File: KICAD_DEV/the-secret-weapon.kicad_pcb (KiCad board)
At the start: 6 copper layers, 100 x 100 mm, 45 parts, among them J1 USB_C_Receptacle_USB2.0_14P, J2 Screw_Terminal_01x02, SW1 SW_Push, SW2 SW_Push, U1 STM32H743VITx, U2 USBLC6-2SC6, U3 LMR33640ADDA, U4 LM1086S-3.3/TR, Y1 8 MHz, Y2 32.768 KHz

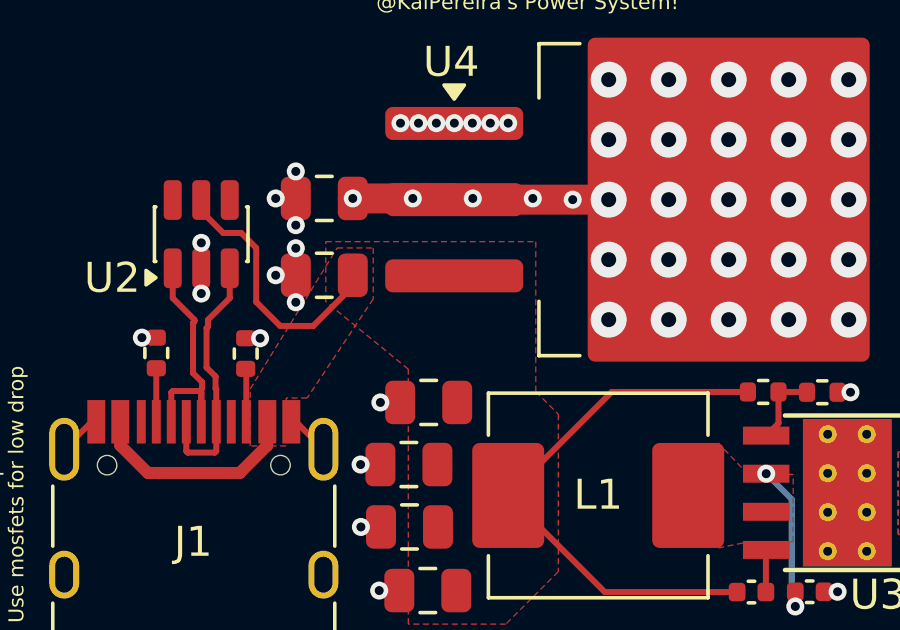
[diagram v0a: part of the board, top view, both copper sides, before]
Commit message: adjusting the power fills and adding the power rails!
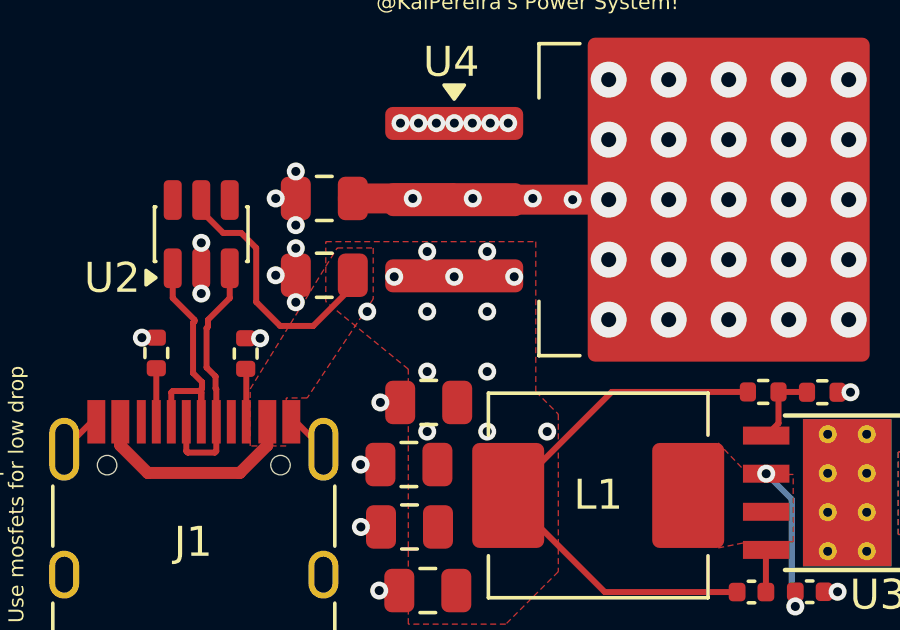
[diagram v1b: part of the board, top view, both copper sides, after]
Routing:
- net +12V: track 1.12 -> 119.7 mm
- net +5V: track 34.6 -> 100.9 mm, vias 0 -> 13
- net +3V3: vias 40 -> 39
- added copper zone on In2.Cu, net +5V
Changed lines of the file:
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@@
-	)
-	(via
-		(at 129.32 164.05)
-		(size 0.6)
-		(drill 0.3)
-		(layers "F.Cu" "B.Cu")
-		(net 9)
 	)
 	(via
@@
 		(net 90)
 	)
+	(via
+		(at 131.8 171.82)
+		(size 0.6)
+		(drill 0.3)
+		(layers "F.Cu" "B.Cu")
+		(net 90)
+	)
+	(via
+		(at 131.8 167.82)
+		(size 0.6)
+		(drill 0.3)
+		(layers "F.Cu" "B.Cu")
+		(net 90)
+	)
+	(via
+		(at 133.8 171.82)
+		(size 0.6)
+		(drill 0.3)
+		(layers "F.Cu" "B.Cu")
+		(net 90)
+	)
+	(via
+		(at 129.8 167.82)
+		(size 0.6)
+		(drill 0.3)
+		(layers "F.Cu" "B.Cu")
+		(net 90)
+	)
+	(via
+		(at 133.8 169.82)
+		(size 0.6)
+		(drill 0.3)
+		(layers "F.Cu" "B.Cu")
+		(net 90)
+	)
+	(via
+		(at 133.8 167.82)
+		(size 0.6)
+		(drill 0.3)
+		(layers "F.Cu" "B.Cu")
+		(net 90)
+	)
+	(via
+		(at 131.8 165.82)
+		(size 0.6)
+		(drill 0.3)
+		(layers "F.Cu" "B.Cu")
+		(net 90)
+	)
+	(via
+		(at 131.8 169.82)
+		(size 0.6)
+		(drill 0.3)
+		(layers "F.Cu" "B.Cu")
+		(net 90)
+	)
+	(via
+		(at 130.7 166.66)
+		(size 0.6)
+		(drill 0.3)
+		(layers "F.Cu" "B.Cu")
+		(net 90)
+	)
+	(via
+		(at 134.7 166.66)
+		(size 0.6)
+		(drill 0.3)
+		(layers "F.Cu" "B.Cu")
+		(net 90)
+	)
+	(via
+		(at 135.8 171.82)
+		(size 0.6)
+		(drill 0.3)
+		(layers "F.Cu" "B.Cu")
+		(net 90)
+	)
+	(via
+		(at 132.7 166.66)
+		(size 0.6)
+		(drill 0.3)
+		(layers "F.Cu" "B.Cu")
+		(net 90)
+	)
+	(via
+		(at 133.8 165.82)
+		(size 0.6)
+		(drill 0.3)
+		(layers "F.Cu" "B.Cu")
+		(net 90)
+	)
+	(segment
+		(start 131.807265 166.66)
+		(end 128.92 163.772735)
+		(width 2)
+		(layer "In2.Cu")
+		(net 90)
+	)
+	(segment
+		(start 124.69 155.52)
+		(end 118.78 155.52)
+		(width 2)
+		(layer "In2.Cu")
+		(net 90)
+	)
+	(segment
+		(start 109.91 146.65)
+		(end 109.91 115.82)
+		(width 2)
+		(layer "In2.Cu")
+		(net 90)
+	)
+	(segment
+		(start 128.92 159.75)
+		(end 128.7 159.53)
+		(width 2)
+		(layer "In2.Cu")
+		(net 90)
+	)
+	(segment
+		(start 134.7 166.66)
+		(end 131.807265 166.66)
+		(width 2)
+		(layer "In2.Cu")
+		(net 90)
+	)
+	(segment
+		(start 118.78 155.52)
+		(end 109.91 146.65)
+		(width 2)
+		(layer "In2.Cu")
+		(net 90)
+	)
+	(segment
+		(start 128.92 163.772735)
+		(end 128.92 159.75)
+		(width 2)
+		(layer "In2.Cu")
+		(net 90)
+	)
+	(segment
+		(start 128.7 159.53)
+		(end 124.69 155.52)
+		(width 2)
+		(layer "In2.Cu")
+		(net 90)
+	)
 	(segment
 		(start 124.221 170.469)
@@
 		(layers "F.Cu" "B.Cu")
 		(free yes)
+		(net 94)
+	)
+	(segment
+		(start 150.9 96.09)
+		(end 115.68 96.09)
+		(width 3)
+		(layer "In2.Cu")
+		(net 94)
+	)
+	(segment
+		(start 156.04 162.75)
+		(end 162.1 156.69)
+		(width 3)
+		(layer "In2.Cu")
+		(net 94)
+	)
+	(segment
+		(start 156.04 165.25)
+		(end 156.04 162.75)
+		(width 3)
+		(layer "In2.Cu")
+		(net 94)
+	)
+	(segment
+		(start 162.1 156.69)
+		(end 162.1 107.29)
+		(width 3)
+		(layer "In2.Cu")
+		(net 94)
+	)
+	(segment
+		(start 162.1 107.29)
+		(end 150.9 96.09)
+		(width 3)
+		(layer "In2.Cu")
+		(net 94)
+	)
+	(segment
+		(start 156.04 162.75)
+		(end 159.54 162.75)
+		(width 3)
+		(layer "In2.Cu")
+		(net 94)
+	)
+	(segment
+		(start 159.54 165.25)
+		(end 156.04 165.25)
+		(width 3)
+		(layer "In2.Cu")
 		(net 94)
 	)
@@
 			(pts
 				(xy 141.5 172.2) (xy 141.5 175.7) (xy 142.5 175.5) (xy 144 175.5) (xy 144 173.25) (xy 142.5 173.25)
-			)
-		)
-	)
-	(zone
-		(net 90)
-		(net_name "+5V")
-		(layer "F.Cu")
-		(hatch edge 0.5)
-		(priority 5)
-		(connect_pads
-			(clearance 0.1)
-		)
-		(min_thickness 0.25)
-		(filled_areas_thickness no)
-		(fill yes
-			(thermal_gap 0.3)
-			(thermal_bridge_width 0.5)
-		)
-		(polygon
-			(pts
-				(xy 125.9 172.3) (xy 125.9 170.4) (xy 128.8 165.7) (xy 130 165.7) (xy 130 167.4) (xy 127.8 170.7)
-				(xy 127.1 170.7) (xy 127.1 172.3)
-			)
-		)
-	)
-	(zone
-		(net 90)
-		(net_name "+5V")
-		(layer "F.Cu")
-		(hatch edge 0.5)
-		(priority 3)
-		(connect_pads
-			(clearance 0.2)
-		)
-		(min_thickness 0.25)
-		(filled_areas_thickness no)
-		(fill yes
-			(thermal_gap 0.15)
-			(thermal_bridge_width 1)
-		)
-		(polygon
-			(pts
-				(xy 135.42 165.49) (xy 135.42 170.49) (xy 136.17 171.24) (xy 136.17 176.49) (xy 134.42 178.24) (xy 131.17 178.24)
-				(xy 131.17 169.74) (xy 128.42 167.49) (xy 128.42 165.49)
 			)
 		)
@@
 	)
 	(zone
+		(net 90)
+		(net_name "+5V")
+		(layers "F.Cu" "In2.Cu")
+		(hatch edge 0.5)
+		(priority 5)
+		(connect_pads
+			(clearance 0.1)
+		)
+		(min_thickness 0.25)
+		(filled_areas_thickness no)
+		(fill yes
+			(thermal_gap 0.3)
+			(thermal_bridge_width 0.5)
+		)
+		(polygon
+			(pts
+				(xy 125.9 172.3) (xy 125.9 170.4) (xy 128.8 165.7) (xy 130 165.7) (xy 130 167.4) (xy 127.8 170.7)
+				(xy 127.1 170.7) (xy 127.1 172.3)
+			)
+		)
+	)
+	(zone
+		(net 90)
+		(net_name "+5V")
+		(layers "F.Cu" "In2.Cu")
+		(hatch edge 0.5)
+		(priority 3)
+		(connect_pads
+			(clearance 0.2)
+		)
+		(min_thickness 0.25)
+		(filled_areas_thickness no)
+		(fill yes
+			(thermal_gap 0.15)
+			(thermal_bridge_width 1)
+		)
+		(polygon
+			(pts
+				(xy 135.42 165.49) (xy 135.42 170.49) (xy 136.17 171.24) (xy 136.17 176.49) (xy 134.42 178.24) (xy 131.17 178.24)
+				(xy 131.17 169.74) (xy 128.42 167.49) (xy 128.42 165.49)
+			)
+		)
+	)
+	(zone
 		(net 1)
 		(net_name "GND")
@@
 		(hatch edge 0.5)
 		(connect_pads
-			(clearance 0.5)
+			(clearance 0.2)
 		)
 		(min_thickness 0.25)
@@
 		(fill yes
 			(thermal_gap 0.5)
-			(thermal_bridge_width 0.5)
+			(thermal_bridge_width 1)
 		)
 		(polygon
@@
 		(hatch edge 0.5)
 		(connect_pads
-			(clearance 0.5)
+			(clearance 0.3)
 		)
 		(min_thickness 0.25)

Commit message: forgot to wire USB data pairs, doing that now!
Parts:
- moved C24 27.7 mm to (125.3, 144.3), turned to 180 degrees
- moved C8 27.3 mm to (123.8, 142.3), turned to 180 degrees
- moved C29 26.9 mm to (126.8, 123.4), turned to -90 degrees
- moved R13 26.9 mm to (140.6, 122.1), turned to 0 degrees
- moved C7 26.8 mm to (138.5, 147.1), turned to -90 degrees
- moved R14 26.6 mm to (146.5, 127.9), turned to -90 degrees
- moved SW1 25.9 mm to (143.2, 124.3), turned to 180 degrees
- moved C21 25.5 mm to (140.5, 145.6), turned to -90 degrees
- moved Y1 23.3 mm to (130.3, 123.4), turned to 0 degrees
- moved C25 22.4 mm to (123.8, 131.8), turned to 180 degrees
- moved C27 22.4 mm to (139.9, 124.2), turned to 90 degrees
- moved C28 21.7 mm to (133.8, 123.4), turned to -90 degrees
- moved SW2 21.0 mm to (143.2, 128.0), turned to 0 degrees
- moved C30 19.5 mm to (138.9, 125.4), turned to -90 degrees
- moved C9 19.5 mm to (128.2, 127.0), turned to 90 degrees
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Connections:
- U1 pad 70: unconnected-(U1-PA11-Pad70) -> D-
- U1 pad 71: unconnected-(U1-PA12-Pad71) -> D+
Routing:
- net USB_D-: track 8.57 -> 2.99 mm
- net USB_D+: track 8.57 -> 2.99 mm
- net +5V: track 100.9 -> 100.0 mm

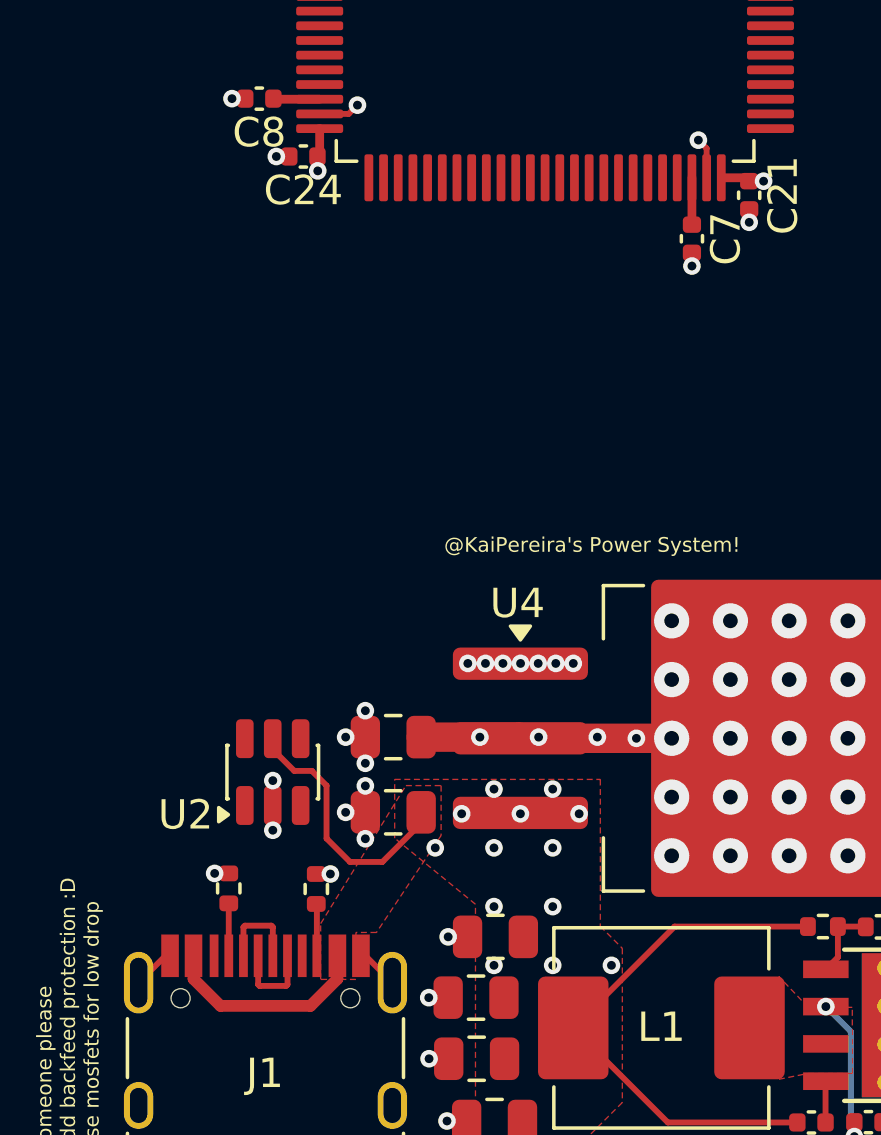
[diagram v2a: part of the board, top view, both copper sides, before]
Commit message: added some more warnings around the board and routed the USB data pairs!
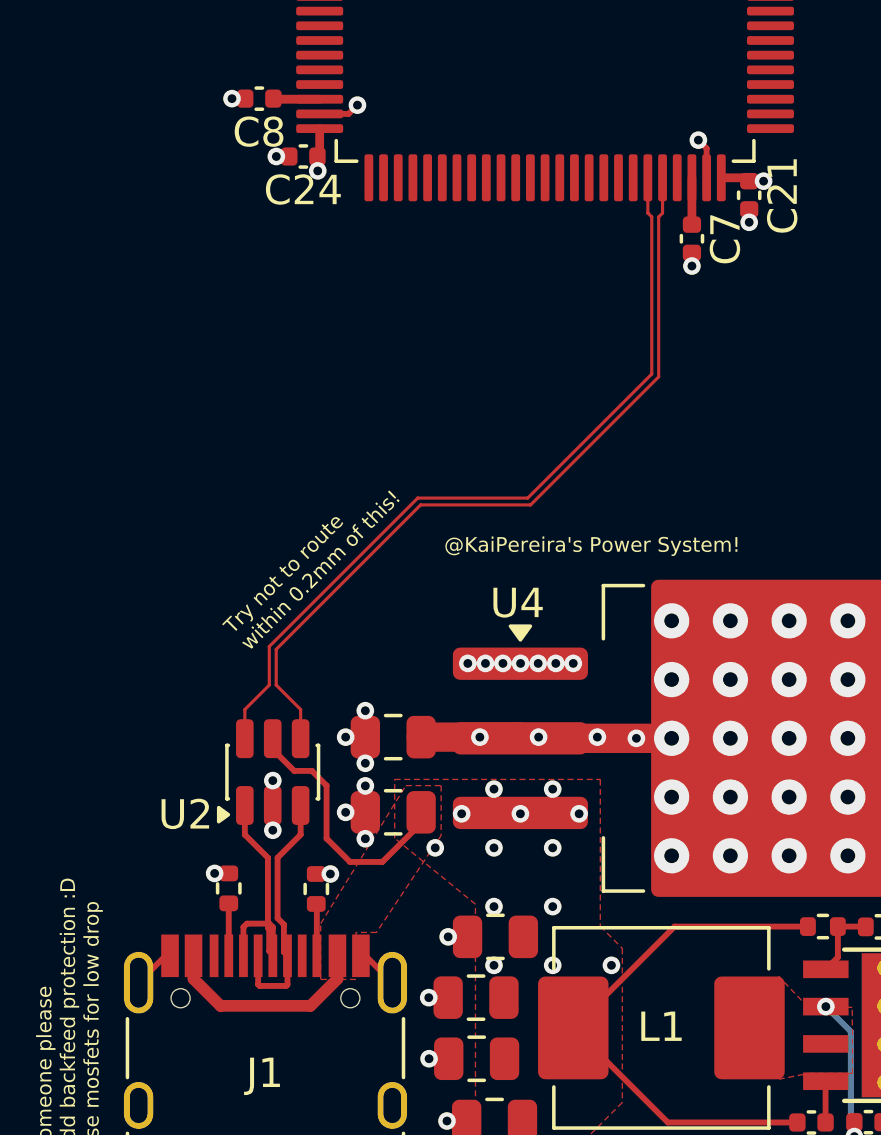
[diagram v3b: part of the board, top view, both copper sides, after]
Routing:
- net D-: track 0.00 -> 27.1 mm
- net D+: track 0.00 -> 27.1 mm
- net USB_D-: track 2.99 -> 8.59 mm
- net USB_D+: track 2.99 -> 8.58 mm
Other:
- board text added: "Try not to route within 0.2mm of this!"
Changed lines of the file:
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@@
 	)
 	(gr_text "Someone please \nadd backfeed protection :D\nUse mosfets for low drop"
-		(locked yes)
 		(at 118.4 178.2 90)
 		(layer "F.SilkS")
@@
 	)
 	(gr_text "Beginners can maybe \nadd some power LED's"
-		(locked yes)
 		(at 149.5 169.5 90)
 		(layer "F.SilkS")
@@
 	)
 	(gr_text "@KaiPereira's Power System!"
-		(locked yes)
 		(at 130.1 157.8 0)
 		(layer "F.SilkS")
@@
 		)
 	)
+	(gr_text "Try not to route \nwithin 0.2mm of this!"
+		(at 123.51 161.17 45)
+		(layer "F.SilkS")
+		(effects
+			(font
+				(size 0.5 0.5)
+				(thickness 0.1)
+			)
+			(justify left bottom)
+		)
+	)
 	(segment
 		(start 130.54 127.1)
@@
 	)
 	(segment
+		(start 124.648 171.373)
+		(end 124.648 170.432138)
+		(width 0.2)
+		(layer "F.Cu")
+		(net 87)
+	)
+	(segment
 		(start 123.77 172.472)
 		(end 123.77 171.495)
@@
 	)
 	(segment
+		(start 125.2175 167.371251)
+		(end 125.2175 166.3775)
+		(width 0.2)
+		(layer "F.Cu")
+		(net 87)
+	)
+	(segment
 		(start 124.77 171.495)
 		(end 124.77 172.472)
+		(width 0.2)
+		(layer "F.Cu")
+		(net 87)
+	)
+	(segment
+		(start 124.43198 170.216118)
+		(end 124.43198 168.156771)
+		(width 0.2)
+		(layer "F.Cu")
+		(net 87)
+	)
+	(segment
+		(start 124.77 171.495)
+		(end 124.648 171.373)
+		(width 0.2)
+		(layer "F.Cu")
+		(net 87)
+	)
+	(segment
+		(start 124.648 170.432138)
+		(end 124.43198 170.216118)
+		(width 0.2)
+		(layer "F.Cu")
+		(net 87)
+	)
+	(segment
+		(start 124.43198 168.156771)
+		(end 125.2175 167.371251)
 		(width 0.2)
 		(layer "F.Cu")
@@
 	)
 	(segment
-		(start 124.221 170.469)
-		(end 123.319 170.469)
+		(start 123.388 170.4)
+		(end 123.27 170.518)
 		(width 0.2)
 		(layer "F.Cu")
@@
 	)
 	(segment
-		(start 123.319 170.469)
-		(end 123.27 170.518)
+		(start 123.3175 167.371251)
+		(end 123.3175 166.3775)
+		(width 0.2)
+		(layer "F.Cu")
+		(net 89)
+	)
+	(segment
+		(start 124.27 171.495)
+		(end 124.27 171.457448)
 		(width 0.2)
 		(layer "F.Cu")
@@
 	)
 	(segment
+		(start 124.148 171.335448)
+		(end 124.148 170.542)
+		(width 0.2)
+		(layer "F.Cu")
+		(net 89)
+	)
+	(segment
+		(start 124.27 170.518)
+		(end 124.152 170.4)
+		(width 0.2)
+		(layer "F.Cu")
+		(net 89)
+	)
+	(segment
+		(start 124.104 170.542)
+		(end 124.104 168.157751)
+		(width 0.2)
+		(layer "F.Cu")
+		(net 89)
+	)
+	(segment
 		(start 123.27 170.518)
 		(end 123.27 171.495)
@@
 	)
 	(segment
-		(start 124.27 170.518)
-		(end 124.221 170.469)
+		(start 124.27 171.457448)
+		(end 124.148 171.335448)
 		(width 0.2)
 		(layer "F.Cu")
@@
 	)
 	(segment
+		(start 124.104 168.157751)
+		(end 123.3175 167.371251)
+		(width 0.2)
+		(layer "F.Cu")
+		(net 89)
+	)
+	(segment
+		(start 124.148 170.542)
+		(end 124.104 170.542)
+		(width 0.2)
+		(layer "F.Cu")
+		(net 89)
+	)
+	(segment
+		(start 124.152 170.4)
+		(end 123.388 170.4)
+		(width 0.2)
+		(layer "F.Cu")
+		(net 89)
+	)
+	(segment
+		(start 123.3175 163.108749)
+		(end 124.1504 162.275849)
+		(width 0.1072)
+		(layer "F.Cu")
+		(net 90)
+	)
+	(segment
+		(start 137.1729 146.337901)
+		(end 137.04 146.205001)
+		(width 0.1072)
+		(layer "F.Cu")
+		(net 90)
+	)
+	(segment
+		(start 124.1504 160.963994)
+		(end 129.204394 155.91)
+		(width 0.1072)
+		(layer "F.Cu")
+		(net 90)
+	)
+	(segment
+		(start 137.04 146.205001)
+		(end 137.04 145.005)
+		(width 0.1072)
+		(layer "F.Cu")
+		(net 90)
+	)
+	(segment
+		(start 124.1504 162.275849)
+		(end 124.1504 160.963994)
+		(width 0.1072)
+		(layer "F.Cu")
+		(net 90)
+	)
+	(segment
+		(start 123.3175 164.1025)
+		(end 123.3175 163.108749)
+		(width 0.1072)
+		(layer "F.Cu")
+		(net 90)
+	)
+	(segment
+		(start 132.948788 155.91)
+		(end 137.1729 151.685888)
+		(width 0.1072)
+		(layer "F.Cu")
+		(net 90)
+	)
+	(segment
+		(start 137.1729 151.685888)
+		(end 137.1729 146.337901)
+		(width 0.1072)
+		(layer "F.Cu")
+		(net 90)
+	)
+	(segment
+		(start 129.204394 155.91)
+		(end 132.948788 155.91)
+		(width 0.1072)
+		(layer "F.Cu")
+		(net 90)
+	)
+	(segment
+		(start 124.3846 162.275849)
+		(end 124.3846 161.061006)
+		(width 0.1072)
+		(layer "F.Cu")
+		(net 91)
+	)
+	(segment
+		(start 137.4071 151.7829)
+		(end 137.4071 146.337901)
+		(width 0.1072)
+		(layer "F.Cu")
+		(net 91)
+	)
+	(segment
+		(start 133.0458 156.1442)
+		(end 137.4071 151.7829)
+		(width 0.1072)
+		(layer "F.Cu")
+		(net 91)
+	)
+	(segment
+		(start 124.3846 161.061006)
+		(end 129.301406 156.1442)
+		(width 0.1072)
+		(layer "F.Cu")
+		(net 91)
+	)
+	(segment
+		(start 125.2175 164.1025)
+		(end 125.2175 163.108749)
+		(width 0.1072)
+		(layer "F.Cu")
+		(net 91)
+	)
+	(segment
+		(start 125.2175 163.108749)
+		(end 124.3846 162.275849)
+		(width 0.1072)
+		(layer "F.Cu")
+		(net 91)
+	)
+	(segment
+		(start 129.301406 156.1442)
+		(end 133.0458 156.1442)
+		(width 0.1072)
+		(layer "F.Cu")
+		(net 91)
+	)
+	(segment
+		(start 137.4071 146.337901)
+		(end 137.54 146.205001)
+		(width 0.1072)
+		(layer "F.Cu")
+		(net 91)
+	)
+	(segment
+		(start 137.54 146.205001)
+		(end 137.54 145.005)
+		(width 0.1072)
+		(layer "F.Cu")
+		(net 91)
+	)
+	(segment

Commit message: done with the root PCBgit add .
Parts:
- renumbered SW2 to BOOT, SW1 to RESET
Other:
- board text added: "Core MCU!"
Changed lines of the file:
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@@
 		(tags "SMD SMT crystal")
 		(property "Reference" "Y1"
-			(at 0 -2.5 0)
+			(at 0 0.06 0)
 			(layer "F.SilkS")
 			(effects
@@
 			(at 0 -1.16 90)
 			(layer "F.SilkS")
+			(hide yes)
 			(effects
 				(font
@@
 			(at 0 -1.16 90)
 			(layer "F.SilkS")
+			(hide yes)
 			(effects
 				(font
@@
 			(at 0 -1.43 90)
 			(layer "F.SilkS")
+			(hide yes)
 			(effects
 				(font
@@
 		(descr "http://www.alps.com/prod/info/E/HTML/Tact/SurfaceMount/SKRK/SKRKAHE020.html")
 		(tags "SMD SMT button")
-		(property "Reference" "SW1"
-			(at 0 -2.25 0)
+		(property "Reference" "RESET"
+			(at -6.28 -0.07 0)
 			(layer "F.SilkS")
 			(effects
 				(font
 					(size 1 1)
-					(thickness 0.15)
+					(thickness 0.2)
+					(bold yes)
 				)
 			)
@@
 			(at 0 -1.16 90)
 			(layer "F.SilkS")
+			(hide yes)
 			(effects
 				(font
@@
 			(at 0 -1.16 0)
 			(layer "F.SilkS")
+			(hide yes)
 			(effects
 				(font
@@
 		(descr "http://www.alps.com/prod/info/E/HTML/Tact/SurfaceMount/SKRK/SKRKAHE020.html")
 		(tags "SMD SMT button")
-		(property "Reference" "SW2"
-			(at 0 -2.25 0)
+		(property "Reference" "BOOT"
+			(at 5.98 -0.07 0)
 			(layer "F.SilkS")
 			(effects
 				(font
 					(size 1 1)
-					(thickness 0.15)
+					(thickness 0.2)
+					(bold yes)
 				)
 			)
@@
 		(tags "LQFP QFP")
 		(property "Reference" "U1"
-			(at 0 -9.43 90)
+			(at 0 -0.1 180)
 			(layer "F.SilkS")
 			(effects
@@
 			(at 0 -1.16 90)
 			(layer "F.SilkS")
+			(hide yes)
 			(effects
 				(font
@@
 			(at 0 -1.16 90)
 			(layer "F.SilkS")
+			(hide yes)
 			(effects
 				(font
@@
 			(at 0 -1.16 90)
 			(layer "F.SilkS")
+			(hide yes)
 			(effects
 				(font
@@
 			(at 0 -1.16 90)
 			(layer "F.SilkS")
+			(hide yes)
 			(effects
 				(font
@@
 			(at 0 -1.16 90)
 			(layer "F.SilkS")
+			(hide yes)
 			(effects
 				(font
@@
 			(at 0 -1.17 0)
 			(layer "F.SilkS")
+			(hide yes)
 			(effects
 				(font
@@
 		(tags "SMD SMT Crystal")
 		(property "Reference" "Y2"
-			(at 0 -2 0)
+			(at 0 -0.06 0)
 			(layer "F.SilkS")
 			(effects
@@
 			(at 0 -1.16 0)
 			(layer "F.SilkS")
+			(hide yes)
 			(effects
 				(font
@@
 			(at 0 -1.16 90)
 			(layer "F.SilkS")
+			(hide yes)
 			(effects
 				(font
@@
 			(at 0 -1.16 0)
 			(layer "F.SilkS")
+			(hide yes)
 			(effects
 				(font
@@
 			(at 0 -1.16 0)
 			(layer "F.SilkS")
+			(hide yes)
 			(effects
 				(font
@@
 			(at 0 -1.17 90)
 			(layer "F.SilkS")
+			(hide yes)
 			(effects
 				(font
@@
 			(at 0 -1.16 90)
 			(layer "F.SilkS")
+			(hide yes)
 			(effects
 				(font
@@
 			)
 			(justify left bottom)
+		)
+	)
+	(gr_text "Core MCU!"
+		(at 127.6 143.7 0)
+		(layer "F.SilkS")
+		(effects
+			(font
+				(size 1 1)
+				(thickness 0.2)
+				(bold yes)
+			)
+			(justify left bottom)

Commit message: adding some instructions inside of the schematic!
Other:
- board text added: "Try not to route (red) within 0.2mm of this!"
- board text removed: "Try not to route within 0.2mm of this!"
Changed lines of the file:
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@@
 		)
 	)
-	(gr_text "Try not to route \nwithin 0.2mm of this!"
+	(gr_text "Try not to route (red)\nwithin 0.2mm of this!"
 		(at 123.51 161.17 45)
 		(layer "F.SilkS")
